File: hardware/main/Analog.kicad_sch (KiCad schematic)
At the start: 55 parts, among them J301 Overvoltage_protection, J302 Rad_sensor, J303 Mos_temp, J304 Mos_temp, U301 INA823DT, U302 INA823DT, U303 INA293A4, U304 INA293A4, U305 TL7726IDR_1

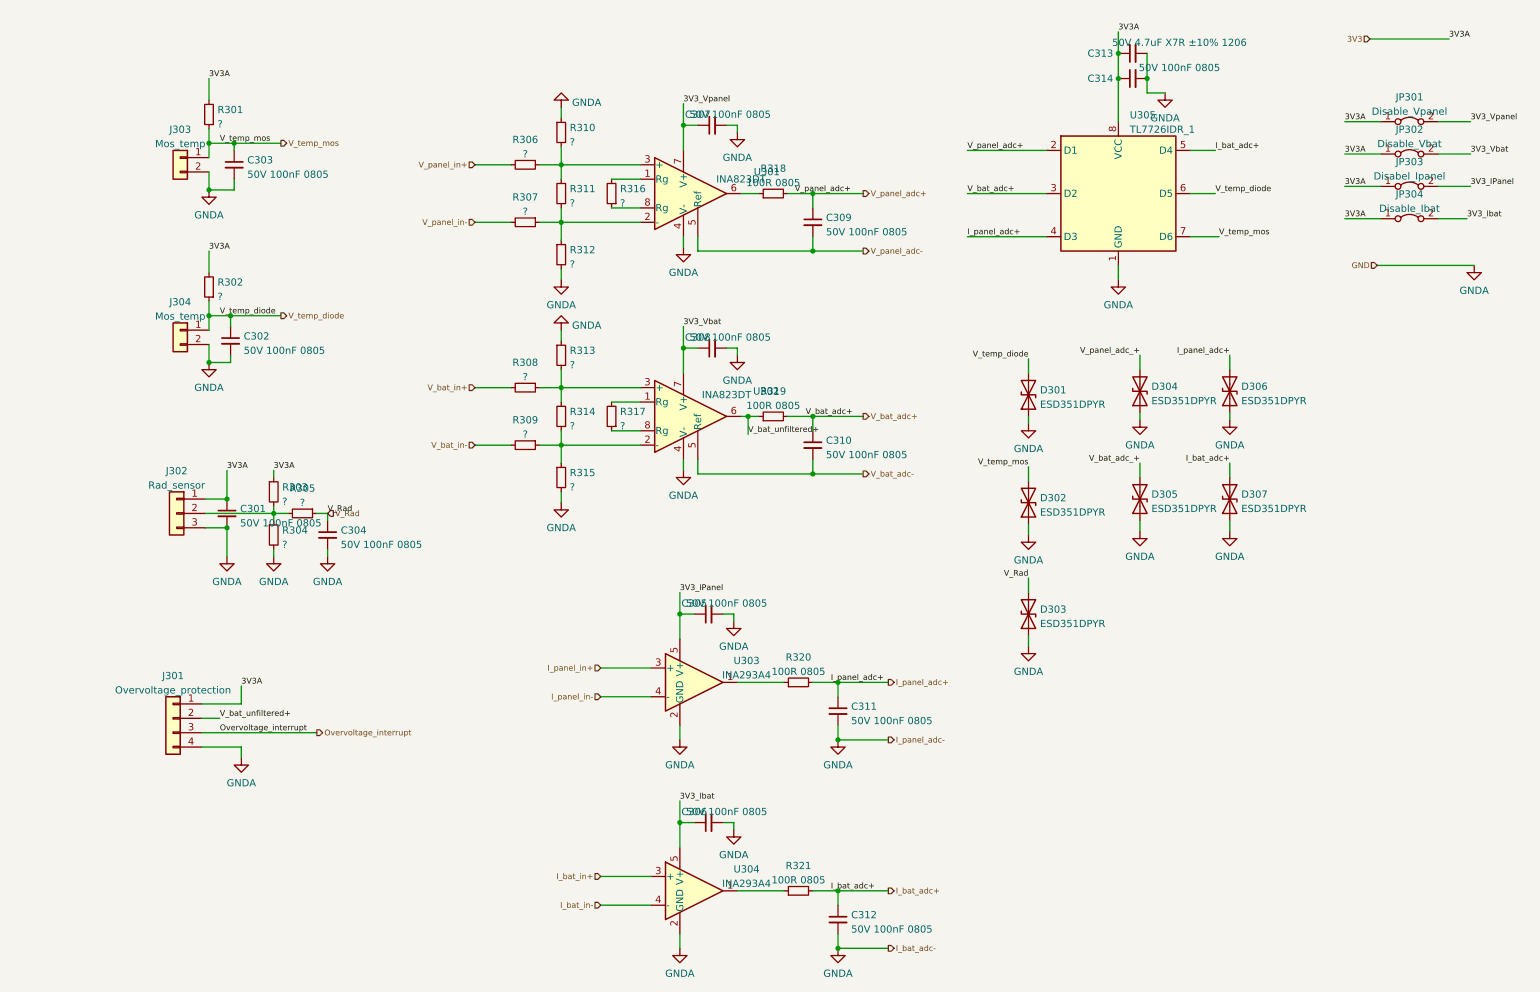
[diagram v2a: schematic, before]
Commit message: Schematics: Sym table and libs updated
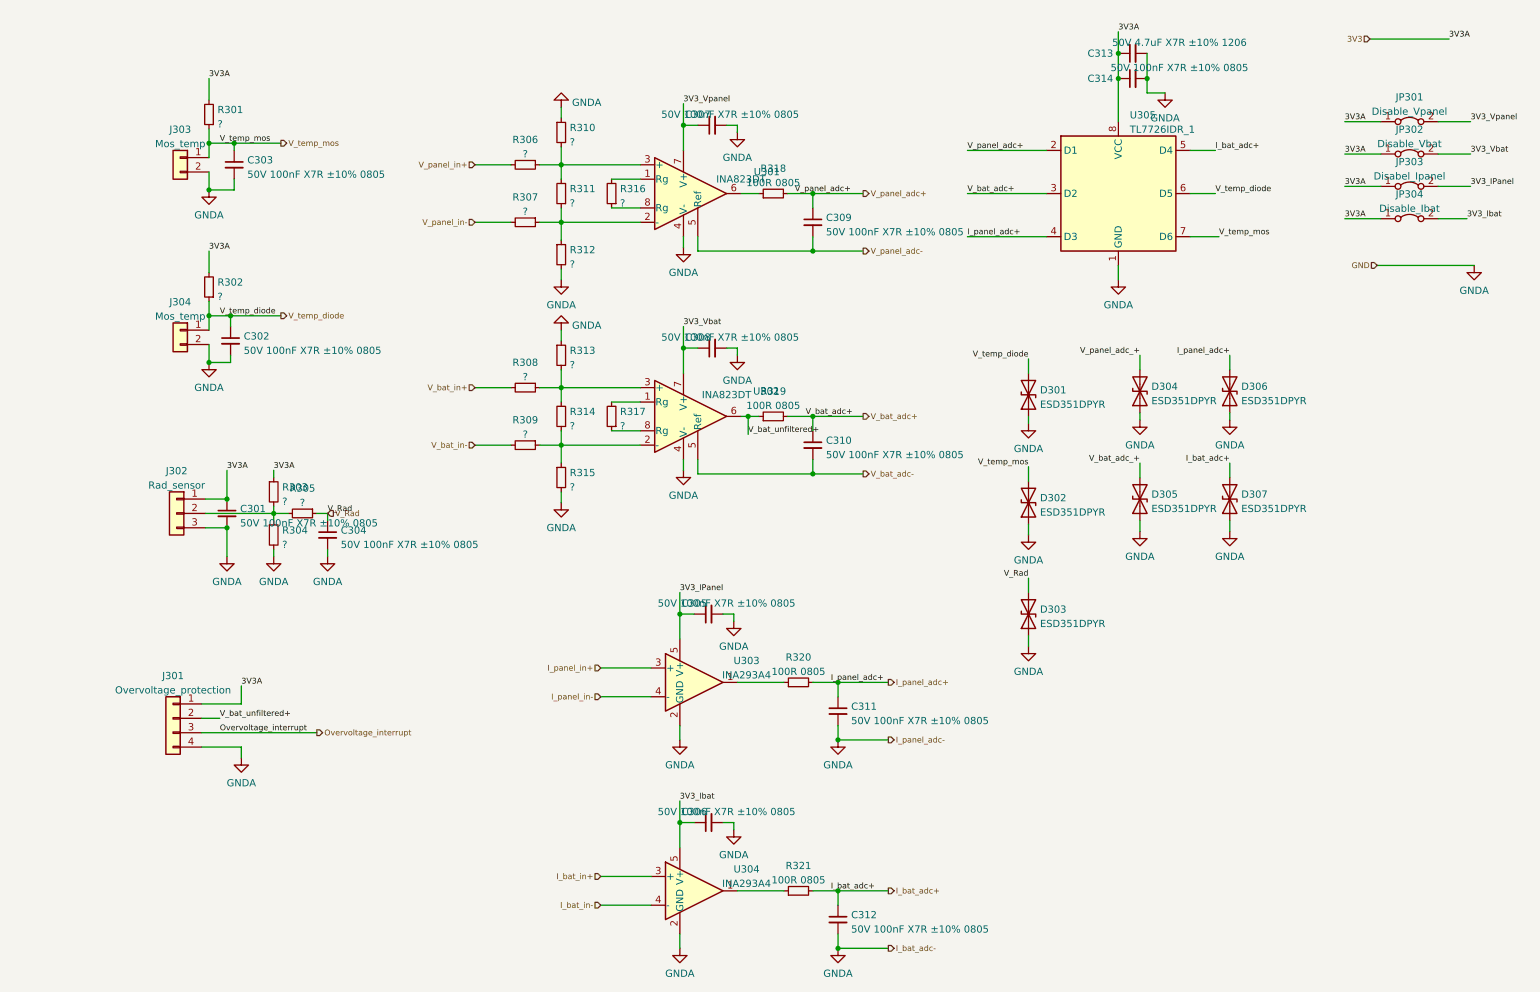
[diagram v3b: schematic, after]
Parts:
- C301, C302, C303, C304, C305, C306, C307, C308, C309, C310, C311, C312, C314: value 50V 100nF 0805 -> 50V 100nF X7R ±10% 0805
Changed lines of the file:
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@@
       (effects (font (size 1.27 1.27)) (justify left))
     )
-    (property "Value" "50V 100nF 0805" (id 1) (at 68.3641 115.3735 0)
+    (property "Value" "50V 100nF X7R ±10% 0805" (id 1) (at 68.3641 115.3735 0)
       (effects (font (size 1.27 1.27)) (justify left))
     )
@@
       (effects (font (size 1.27 1.27)) (justify left))
     )
-    (property "Value" "50V 100nF 0805" (id 1) (at 154.0891 60.1285 0)
+    (property "Value" "50V 100nF X7R ±10% 0805" (id 1) (at 154.0891 60.1285 0)
       (effects (font (size 1.27 1.27)) (justify left))
     )
@@
       (effects (font (size 1.27 1.27)) (justify left))
     )
-    (property "Value" "50V 100nF 0805" (id 1) (at 51.2191 81.0835 0)
+    (property "Value" "50V 100nF X7R ±10% 0805" (id 1) (at 51.2191 81.0835 0)
       (effects (font (size 1.27 1.27)) (justify left))
     )
@@
       (effects (font (size 1.27 1.27)) (justify left))
     )
-    (property "Value" "50V 100nF 0805" (id 1) (at 50.5841 111.5635 0)
+    (property "Value" "50V 100nF X7R ±10% 0805" (id 1) (at 50.5841 111.5635 0)
       (effects (font (size 1.27 1.27)) (justify left))
     )
@@
       (effects (font (size 1.27 1.27)) (justify left))
     )
-    (property "Value" "50V 100nF 0805" (id 1) (at 158.5341 183.3185 0)
+    (property "Value" "50V 100nF X7R ±10% 0805" (id 1) (at 158.5341 183.3185 0)
       (effects (font (size 1.27 1.27)) (justify left))
     )
@@
       (effects (font (size 1.27 1.27)) (justify left))
     )
-    (property "Value" "50V 100nF 0805" (id 1) (at 51.8541 49.9685 0)
+    (property "Value" "50V 100nF X7R ±10% 0805" (id 1) (at 51.8541 49.9685 0)
       (effects (font (size 1.27 1.27)) (justify left))
     )
@@
       (effects (font (size 1.27 1.27)) (justify left))
     )
-    (property "Value" "50V 100nF 0805" (id 1) (at 154.0891 99.4985 0)
+    (property "Value" "50V 100nF X7R ±10% 0805" (id 1) (at 154.0891 99.4985 0)
       (effects (font (size 1.27 1.27)) (justify left))
     )
@@
     (in_bom yes) (on_board yes)
     (property "Reference" "C305" (id 0) (at 130.81 125.73 90))
-    (property "Value" "50V 100nF 0805" (id 1) (at 136.525 125.73 90))
+    (property "Value" "50V 100nF X7R ±10% 0805" (id 1) (at 136.525 125.73 90))
     (property "Footprint" "" (id 2) (at 133.35 127.635 0)
       (effects (font (size 1.27 1.27)) hide)
@@
     (in_bom yes) (on_board yes)
     (property "Reference" "C314" (id 0) (at 202.565 33.02 90))
-    (property "Value" "50V 100nF 0805" (id 1) (at 216.535 31.115 90))
+    (property "Value" "50V 100nF X7R ±10% 0805" (id 1) (at 216.535 31.115 90))
     (property "Footprint" "" (id 2) (at 208.28 33.02 0)
       (effects (font (size 1.27 1.27)) hide)
@@
     (in_bom yes) (on_board yes)
     (property "Reference" "C308" (id 0) (at 131.445 78.74 90))
-    (property "Value" "50V 100nF 0805" (id 1) (at 137.16 78.74 90))
+    (property "Value" "50V 100nF X7R ±10% 0805" (id 1) (at 137.16 78.74 90))
     (property "Footprint" "" (id 2) (at 133.985 80.645 0)
       (effects (font (size 1.27 1.27)) hide)
@@
     (in_bom yes) (on_board yes)
     (property "Reference" "C307" (id 0) (at 131.445 39.37 90))
-    (property "Value" "50V 100nF 0805" (id 1) (at 137.16 39.37 90))
+    (property "Value" "50V 100nF X7R ±10% 0805" (id 1) (at 137.16 39.37 90))
     (property "Footprint" "" (id 2) (at 133.985 41.275 0)
       (effects (font (size 1.27 1.27)) hide)
@@
       (effects (font (size 1.27 1.27)) (justify left))
     )
-    (property "Value" "50V 100nF 0805" (id 1) (at 158.5341 146.4885 0)
+    (property "Value" "50V 100nF X7R ±10% 0805" (id 1) (at 158.5341 146.4885 0)
       (effects (font (size 1.27 1.27)) (justify left))
     )
@@
     (in_bom yes) (on_board yes)
     (property "Reference" "C306" (id 0) (at 130.81 162.56 90))
-    (property "Value" "50V 100nF 0805" (id 1) (at 136.525 162.56 90))
+    (property "Value" "50V 100nF X7R ±10% 0805" (id 1) (at 136.525 162.56 90))
     (property "Footprint" "" (id 2) (at 133.35 164.465 0)
       (effects (font (size 1.27 1.27)) hide)

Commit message: Schematics: Run DRC and fix errors and some warnings, also added Zenite kicad library repo as submodule
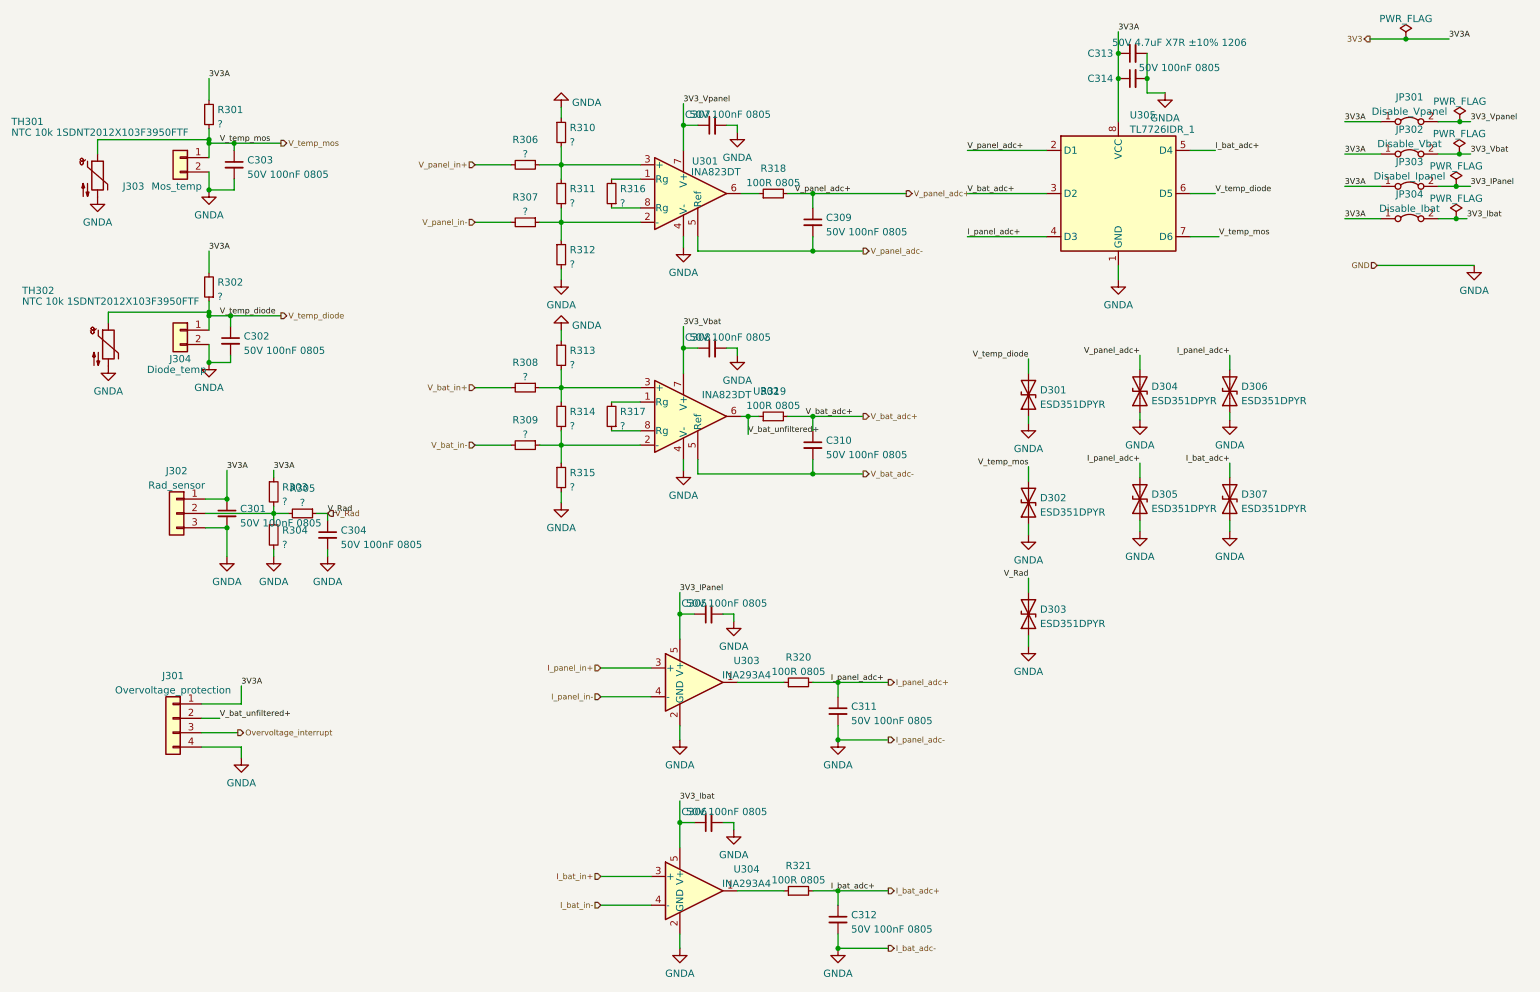
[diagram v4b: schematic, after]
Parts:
- added TH301, TH302: NTC 10k 1SDNT2012X103F3950FTF, Resistor_SMD:R_0805_2012Metric_Pad1.20x1.40mm_HandSolder, symbol Device:Thermistor_NTC
- C301, C302, C303, C304, C305, C306, C307, C308, C309, C310, C311, C312, C314: value 50V 100nF X7R ±10% 0805 -> 50V 100nF 0805; footprint (none) -> Capacitor_SMD:C_0805_2012Metric_Pad1.18x1.45mm_HandSolder
- C313: footprint (none) -> Capacitor_SMD:C_1206_3216Metric_Pad1.33x1.80mm_HandSolder
- D301, D302, D303, D304, D305, D306, D307: footprint (none) -> Diode_SMD:D_0402_1005Metric_Pad0.77x0.64mm_HandSolder
- J301: footprint (none) -> Connector_PinHeader_2.54mm:PinHeader_1x04_P2.54mm_Vertical
- J302: footprint (none) -> Connector_PinHeader_2.54mm:PinHeader_1x03_P2.54mm_Vertical
- J303: footprint (none) -> Connector_PinHeader_2.54mm:PinHeader_1x02_P2.54mm_Vertical
- J304: value Mos_temp -> Diode_temp; footprint (none) -> Connector_PinHeader_2.54mm:PinHeader_1x02_P2.54mm_Vertical
- JP301, JP302, JP303, JP304: footprint (none) -> Jumper:SolderJumper-2_P1.3mm_Open_TrianglePad1.0x1.5mm
- R301, R302, R303, R304, R305, R306, R307, R308, R309, R310, R311, R312, R313, R314, R315, R316, R317, R318, R319, R320, R321: footprint (none) -> Resistor_SMD:R_0805_2012Metric_Pad1.20x1.40mm_HandSolder
- U303, U304: footprint (none) -> Package_TO_SOT_SMD:SOT-23-5_HandSoldering
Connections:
- net V_bat_adc_+ is gone; now on net I_panel_adc+: D305.2 (A2)
- net V_panel_adc_+ is gone; now on net V_panel_adc+: D304.2 (A2)
- net GNDA: now also TH301.2, TH302.2
- net V_temp_diode: now also TH302.1
- net V_temp_mos: now also TH301.1

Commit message: Layout: Organizing components
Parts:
- U301, U302: footprint Package_SO:VSSOP-8_3.0x3.0mm_P0.65mm -> Package_SO:SOIC-8_3.9x4.9mm_P1.27mm
- U305: footprint Package_SON:X2SON-8_1.4x1mm_P0.35mm -> Package_SO:SOIC-8_3.9x4.9mm_P1.27mm
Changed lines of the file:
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@@
     (property "Reference" "U302" (id 0) (at 143.51 88.265 0))
     (property "Value" "INA823DT" (id 1) (at 136.525 88.9 0))
-    (property "Footprint" "Package_SO:VSSOP-8_3.0x3.0mm_P0.65mm" (id 2) (at 128.905 100.33 0)
+    (property "Footprint" "Package_SO:SOIC-8_3.9x4.9mm_P1.27mm" (id 2) (at 128.905 100.33 0)
       (effects (font (size 1.27 1.27)) hide)
     )
@@
     (property "Reference" "U301" (id 0) (at 132.715 47.625 0))
     (property "Value" "INA823DT" (id 1) (at 134.62 49.53 0))
-    (property "Footprint" "Package_SO:VSSOP-8_3.0x3.0mm_P0.65mm" (id 2) (at 128.905 60.96 0)
+    (property "Footprint" "Package_SO:SOIC-8_3.9x4.9mm_P1.27mm" (id 2) (at 128.905 60.96 0)
       (effects (font (size 1.27 1.27)) hide)
     )
@@
       (effects (font (size 1.27 1.27)) (justify left))
     )
-    (property "Footprint" "Package_SON:X2SON-8_1.4x1mm_P0.35mm" (id 2) (at 181.61 66.04 0)
-      (effects (font (size 1.27 1.27)) hide)
-    )
-    (property "Datasheet" "http://www.ti.com/lit/ds/symlink/tpd4s1394.pdf" (id 3) (at 203.2 54.61 0)
-      (effects (font (size 1.27 1.27)) hide)
-    )
+    (property "Footprint" "Package_SO:SOIC-8_3.9x4.9mm_P1.27mm" (id 2) (at 181.61 66.04 0)
+      (effects (font (size 1.27 1.27)) hide)
+    )
+    (property "Datasheet" "https://www.ti.com/lit/ds/symlink/tl7726.pdf?ts=1667512240395&ref_url=https%253A%252F%252Fwww.ti.com%252Fproduct%252FTL7726%252Fpart-details%252FTL7726IDR%253FkeyMatch%253DTL7726IDR" (id 3) (at 203.2 54.61 0)
+      (effects (font (size 1.27 1.27)) hide)
+    )

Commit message: Schematics: Add STM32 comparator for Battery OverVoltage
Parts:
- added R322, R323: NC, Resistor_SMD:R_0805_2012Metric_Pad1.20x1.40mm_HandSolder, symbol Device:R_Small
- added R324, R325: ?, Resistor_SMD:R_0805_2012Metric_Pad1.20x1.40mm_HandSolder, symbol Device:R_Small
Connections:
- net V_bat_adc- is gone; now on net GNDA: C310.2, U302.5 (Ref)
- net V_panel_adc- is gone; now on net GNDA: C309.2, U301.5 (Ref)
- net 3V3: now also R322.2, R324.2
- net GNDA: now also R323.1, R325.1
- net Overvoltage_interrupt renamed Vbat_comp_in_EXT
- new net Vbat_comp: R324.1, R325.2
- new net Vbat_comp_EXT: R322.1, R323.2
